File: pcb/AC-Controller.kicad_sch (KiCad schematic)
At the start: 30 parts, among them J1 Serial, Q1 2N7002, SW1 Mode, SW2 Value, U1 ESP32-WROOM-32

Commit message: style: schematics cleanup
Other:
- note added: "Battery Measurement Voltage Devider"
- note added: "Display"
- note added: "ESP32"
- note added: "Rotary Encoders"
- moved on the sheet: C1, C13, C2, C3, D1, DS1, J1, Q1, R1, R10, R11, R24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

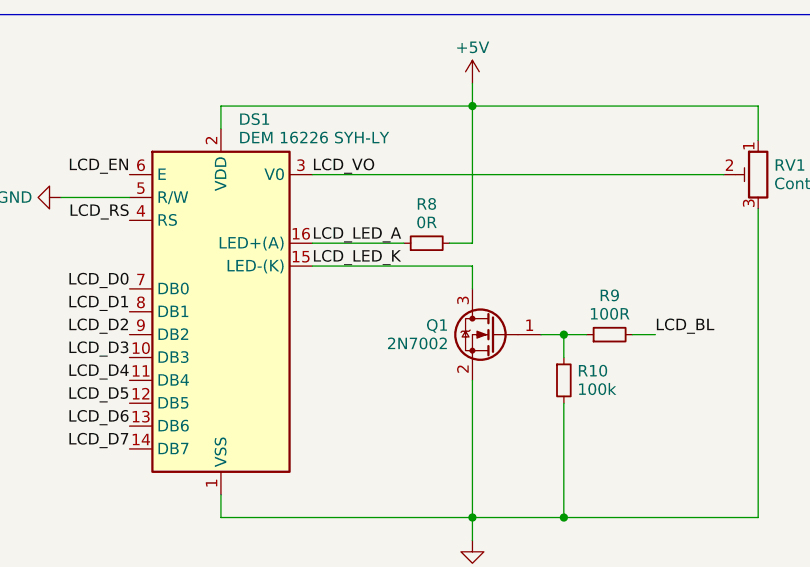
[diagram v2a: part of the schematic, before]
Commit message: feat: add battery protection
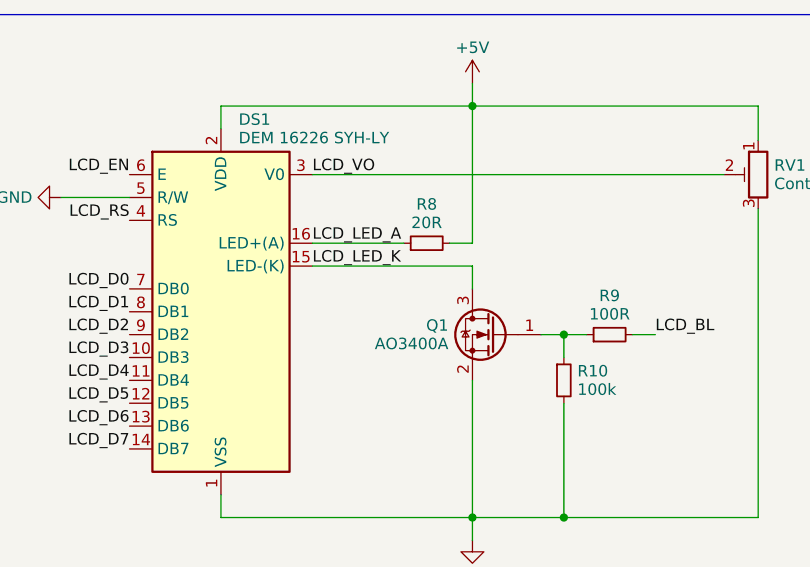
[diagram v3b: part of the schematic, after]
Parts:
- removed Q1: 2N7002, Package_TO_SOT_SMD:SOT-23, symbol Transistor_FET:2N7002
- added Q1: AO3400A, Package_TO_SOT_SMD:SOT-23, symbol Transistor_FET:AO3400A
- R8: value 0R -> 20R; LCSC C21189 -> C22950
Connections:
- net GND: now also Q1.2 (S)
- net LCD_LED_K: now also Q1.3 (D)
- net at R10.1, R9.1: now also Q1.1 (G)
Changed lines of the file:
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@@
       (effects (font (size 1.27 1.27)))
     )
-    (property "Value" "0R" (at 209.55 113.3014 90)
+    (property "Value" "20R" (at 209.55 113.3014 90)
       (effects (font (size 1.27 1.27)))
     )
@@
       (effects (font (size 1.27 1.27)) hide)
     )
-    (property "LCSC" "C21189" (at 209.55 115.57 0)
+    (property "LCSC" "C22950" (at 209.55 115.57 0)
       (effects (font (size 1.27 1.27)) hide)
     )
@@
     )
   )
+  (symbol (lib_id "Transistor_FET:AO3400A") (at 217.17 125.73 0) (mirror y) (unit 1)
+    (in_bom yes) (on_board yes) (dnp no) (fields_autoplaced)
+    (property "Reference" "Q1" (at 211.9631 124.706 0)
+      (effects (font (size 1.27 1.27)) (justify left))
+    )
+    (property "Value" "AO3400A" (at 211.9631 126.754 0)
+      (effects (font (size 1.27 1.27)) (justify left))
+    )
+    (property "Footprint" "Package_TO_SOT_SMD:SOT-23" (at 212.09 127.635 0)
+      (effects (font (size 1.27 1.27) italic) (justify left) hide)
+    )
+    (property "Datasheet" "http://www.aosmd.com/pdfs/datasheet/AO3400A.pdf" (at 217.17 125.73 0)
+      (effects (font (size 1.27 1.27)) (justify left) hide)
+    )
+    (property "LCSC" "C20917" (at 217.17 125.73 0)
+      (effects (font (size 1.27 1.27)) hide)
+    )
+    (pin "1")
+    (pin "2")
+    (pin "3")
+    (instances
+      (project "AC-Controller"
+        (path "/a9b77c2b-ed0c-4412-867d-4d65898d0fc4"
+          (reference "Q1") (unit 1)
+        )
+      )
+    )
+  )
   (symbol (lib_id "Device:R_Small") (at 232.41 48.26 0) (unit 1)
     (in_bom yes) (on_board yes) (dnp no) (fields_autoplaced)
@@
         )
       )
-    )
-  )
-  (symbol (lib_id "Transistor_FET:2N7002") (at 217.17 125.73 0) (mirror y) (unit 1)
-    (in_bom yes) (on_board yes) (dnp no) (fields_autoplaced)
-    (property "Reference" "Q1" (at 211.963 124.706 0)
-      (effects (font (size 1.27 1.27)) (justify left))
-    )
-    (property "Value" "2N7002" (at 211.963 126.754 0)
-      (effects (font (size 1.27 1.27)) (justify left))
-    )
-    (property "Footprint" "Package_TO_SOT_SMD:SOT-23" (at 212.09 127.635 0)
-      (effects (font (size 1.27 1.27) italic) (justify left) hide)
-    )
-    (property "Datasheet" "https://www.onsemi.com/pub/Collateral/NDS7002A-D.PDF" (at 217.17 125.73 0)
-      (effects (font (size 1.27 1.27)) (justify left) hide)
-    )
-    (property "LCSC" "C8545" (at 217.17 125.73 0)
-      (effects (font (size 1.27 1.27)) hide)
-    )
-    (pin "1")
-    (pin "2")
-    (pin "3")
-    (instances
-      (project "AC-Controller"
-        (path "/a9b77c2b-ed0c-4412-867d-4d65898d0fc4"
-          (reference "Q1") (unit 1)
-        )
-      )

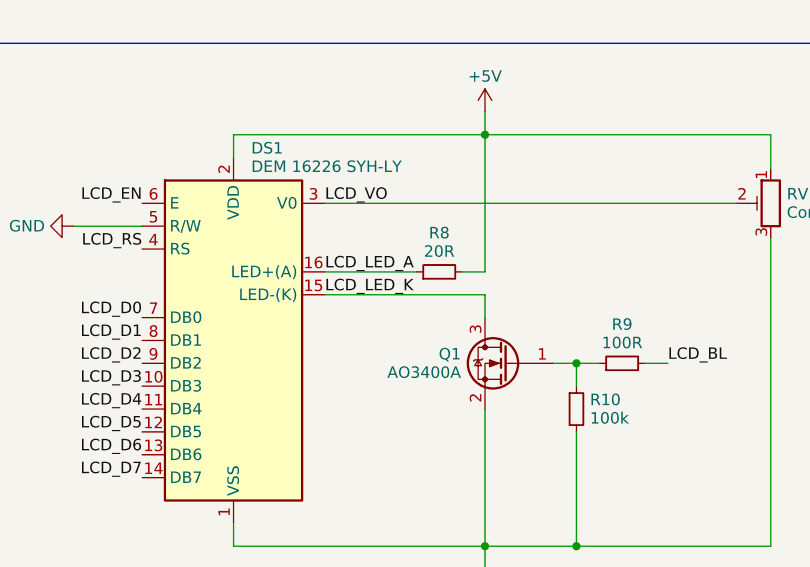
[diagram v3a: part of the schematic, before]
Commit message: feat: add reverse polarity protection for battery input
just to make sure a reverse connected battery won't kill the circuit
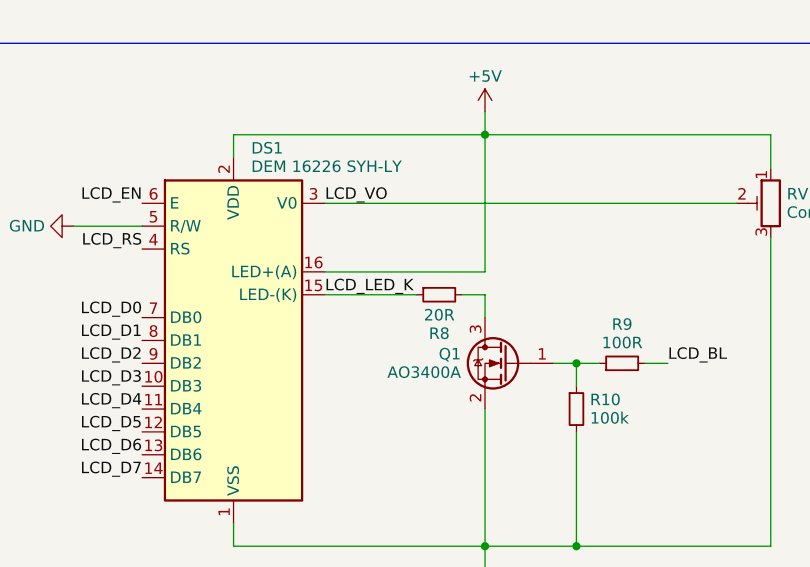
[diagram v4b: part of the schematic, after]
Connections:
- net +5V: now also DS1.16 (LED+(A)); no longer R8.2
- net LCD_LED_K: now also R8.1; no longer Q1.3 (D)
- removed net LCD_LED_A: DS1.16 (LED+(A)), R8.1
- new net: Q1.3 (D), R8.2
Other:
- moved on the sheet: R8
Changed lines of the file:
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@@
-    (stroke (width 0) (type default))
-  )
-  (wire (pts (xy 212.09 115.57) (xy 214.63 115.57))
     (stroke (width 0) (type default))
   )
@@
     (stroke (width 0) (type default))
   )
+  (wire (pts (xy 196.85 118.11) (xy 207.01 118.11))
+    (stroke (width 0) (type default))
+  )
   (wire (pts (xy 161.29 53.34) (xy 179.07 53.34))
     (stroke (width 0) (type default))
@@
     (stroke (width 0) (type default))
   )
+  (wire (pts (xy 212.09 118.11) (xy 214.63 118.11))
+    (stroke (width 0) (type default))
+  )
   (wire (pts (xy 158.75 53.34) (xy 161.29 53.34))
     (stroke (width 0) (type default))
@@
     (stroke (width 0) (type default))
   )
-  (wire (pts (xy 214.63 118.11) (xy 196.85 118.11))
-    (stroke (width 0) (type default))
-  )
   (wire (pts (xy 97.79 53.34) (xy 97.79 50.8))
     (stroke (width 0) (type default))
@@
     (stroke (width 0) (type default))
   )
-  (wire (pts (xy 196.85 115.57) (xy 207.01 115.57))
-    (stroke (width 0) (type default))
-  )
   (wire (pts (xy 30.48 43.18) (xy 30.48 45.72))
     (stroke (width 0) (type default))
@@
   )
   (wire (pts (xy 105.41 157.48) (xy 105.41 163.83))
+    (stroke (width 0) (type default))
+  )
+  (wire (pts (xy 196.85 115.57) (xy 214.63 115.57))
     (stroke (width 0) (type default))
   )
@@
   (label "Encoder2_A" (at 220.98 53.34 180) (fields_autoplaced)
     (effects (font (size 1.27 1.27)) (justify right bottom))
-  )
-  (label "LCD_LED_A" (at 196.85 115.57 0) (fields_autoplaced)
-    (effects (font (size 1.27 1.27)) (justify left bottom))
   )
   (label "LCD_D7" (at 85.09 86.36 0) (fields_autoplaced)
@@
     )
   )
-  (symbol (lib_id "Device:R_Small") (at 209.55 115.57 90) (unit 1)
-    (in_bom yes) (on_board yes) (dnp no) (fields_autoplaced)
-    (property "Reference" "R8" (at 209.55 111.2534 90)
+  (symbol (lib_id "Device:R_Small") (at 209.55 118.11 90) (mirror x) (unit 1)
+    (in_bom yes) (on_board yes) (dnp no)
+    (property "Reference" "R8" (at 209.55 122.4266 90)
       (effects (font (size 1.27 1.27)))
     )
-    (property "Value" "20R" (at 209.55 113.3014 90)
+    (property "Value" "20R" (at 209.55 120.3786 90)
       (effects (font (size 1.27 1.27)))
     )
-    (property "Footprint" "Resistor_SMD:R_0603_1608Metric" (at 209.55 115.57 0)
-      (effects (font (size 1.27 1.27)) hide)
-    )
-    (property "Datasheet" "~" (at 209.55 115.57 0)
-      (effects (font (size 1.27 1.27)) hide)
-    )
-    (property "LCSC" "C22950" (at 209.55 115.57 0)
-      (effects (font (size 1.27 1.27)) hide)
-    )
+    (property "Footprint" "Resistor_SMD:R_0603_1608Metric" (at 209.55 118.11 0)
+      (effects (font (size 1.27 1.27)) hide)
+    )
+    (property "Datasheet" "~" (at 209.55 118.11 0)
+      (effects (font (size 1.27 1.27)) hide)
+    )
+    (property "LCSC" "C22950" (at 209.55 118.11 0)
+      (effects (font (size 1.27 1.27)) hide)
+    )

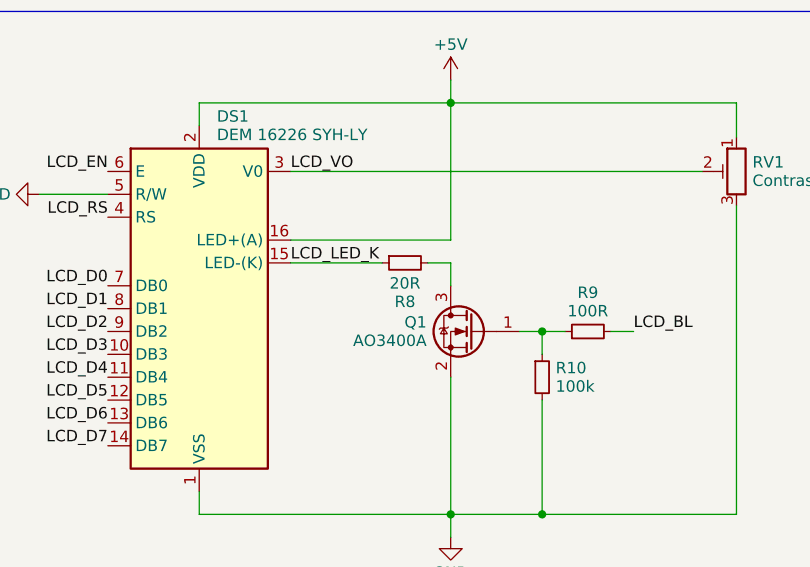
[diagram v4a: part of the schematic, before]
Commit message: fix: add missing JLC part numbers
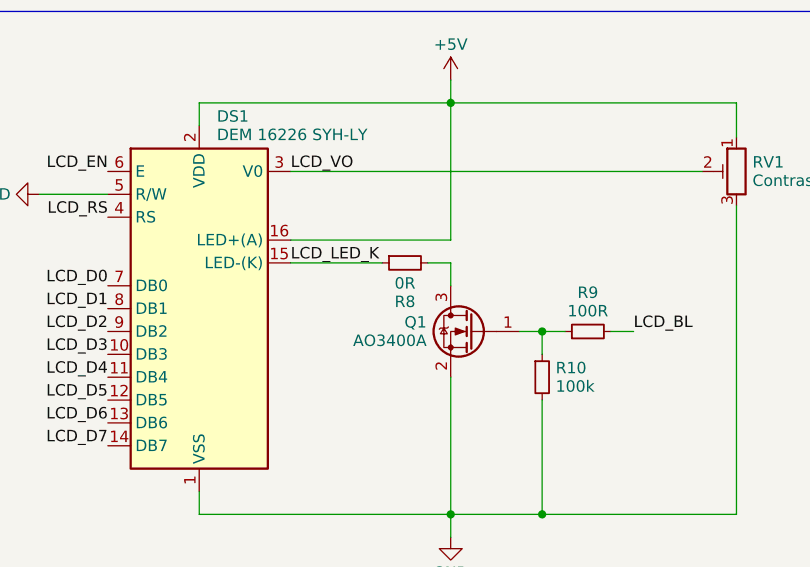
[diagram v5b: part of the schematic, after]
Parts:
- R8: value 20R -> 0R; LCSC C22950 -> C21189
- U1: LCSC (none) -> C82899
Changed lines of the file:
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@@
       (effects (font (size 1.27 1.27)))
     )
-    (property "Value" "20R" (at 209.55 120.3786 90)
+    (property "Value" "0R" (at 209.55 120.3786 90)
       (effects (font (size 1.27 1.27)))
     )
@@
       (effects (font (size 1.27 1.27)) hide)
     )
-    (property "LCSC" "C22950" (at 209.55 118.11 0)
+    (property "LCSC" "C21189" (at 209.55 118.11 0)
       (effects (font (size 1.27 1.27)) hide)
     )
@@
       (effects (font (size 1.27 1.27)) hide)
     )
+    (property "LCSC" "C82899" (at 69.85 76.2 0)
+      (effects (font (size 1.27 1.27)) hide)
+    )

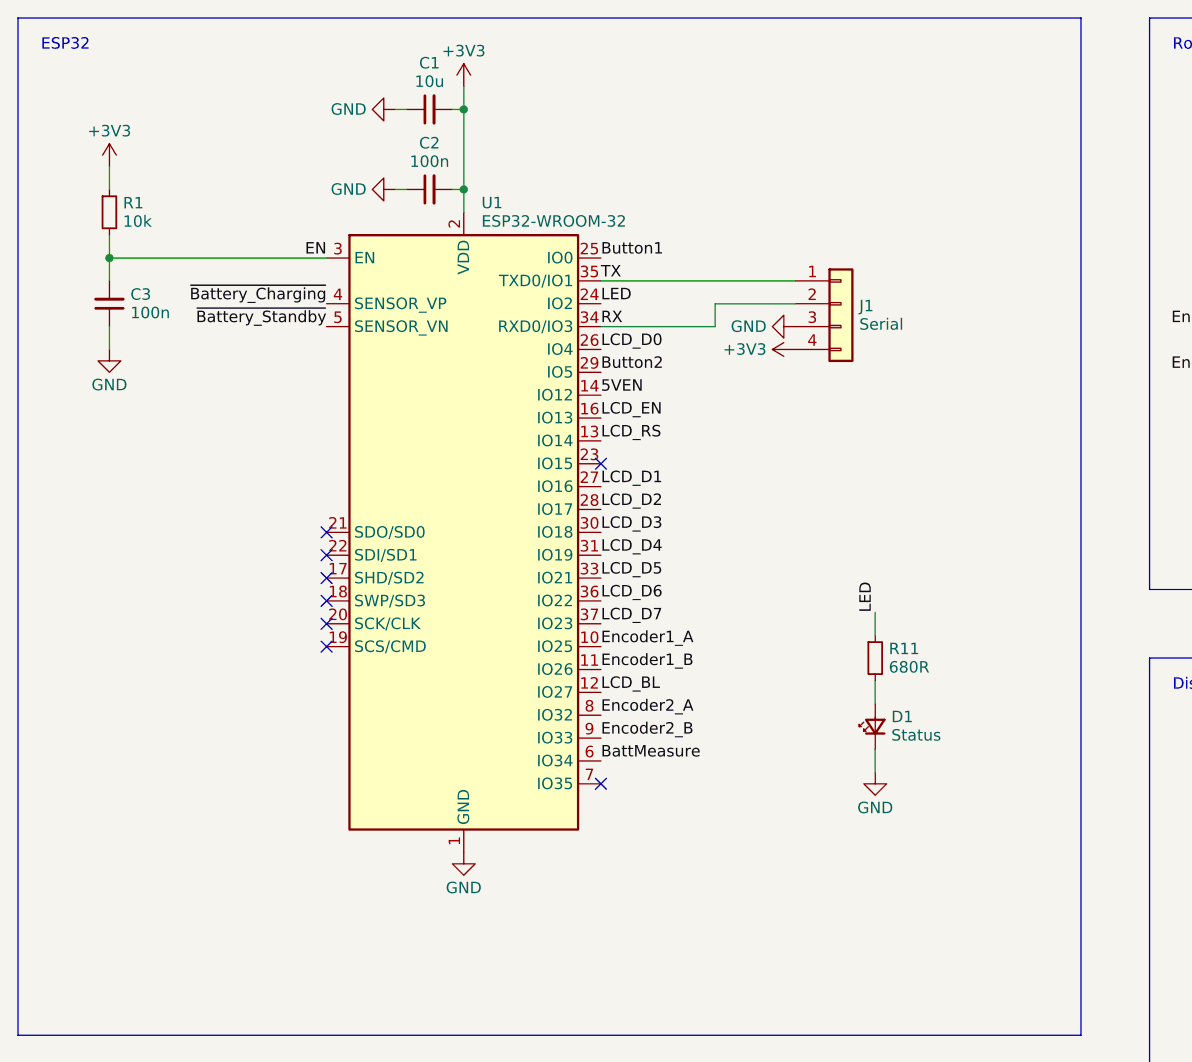
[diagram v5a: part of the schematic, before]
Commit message: feat: add Reset button
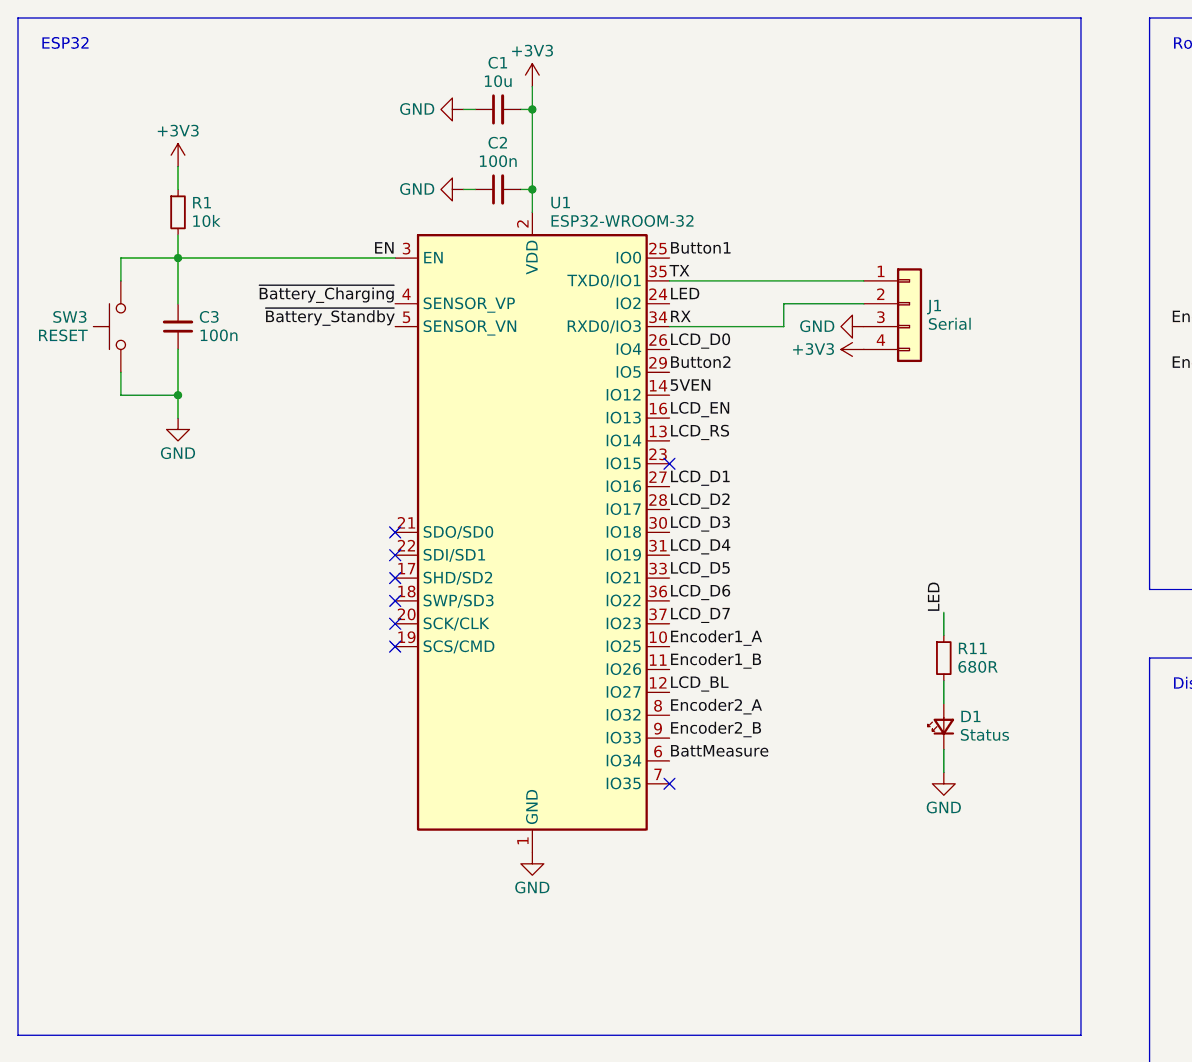
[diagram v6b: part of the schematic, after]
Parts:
- added SW3: RESET, Button_Switch_SMD:SW_Push_1P1T_XKB_TS-1187A, symbol Switch:SW_Push
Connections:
- net EN: now also SW3.2
- net GND: now also SW3.1
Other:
- moved on the sheet: C1, C2, C3, D1, J1, R1, R11, U1
